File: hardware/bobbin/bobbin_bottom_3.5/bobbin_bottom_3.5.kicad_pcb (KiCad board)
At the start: 2 copper layers, 78.5 x 8.5 mm, 2 parts

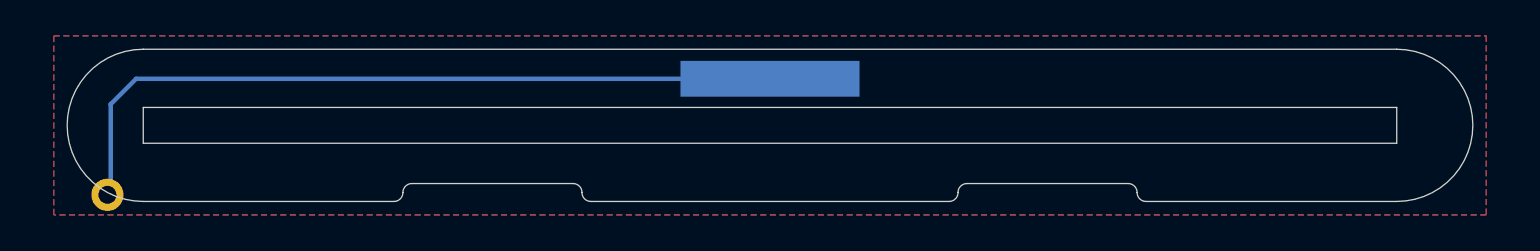
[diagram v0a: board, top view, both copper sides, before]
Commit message: Preamp, Tone Block, Passive, and Bobbin Panel updates
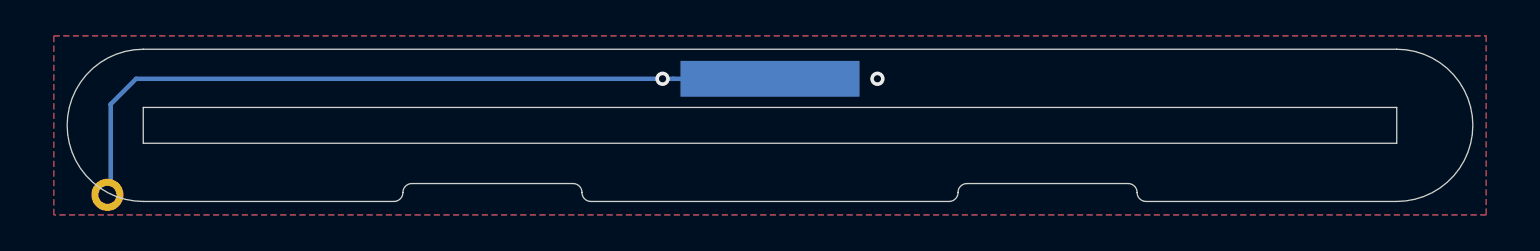
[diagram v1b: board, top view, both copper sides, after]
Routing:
- net GND: vias 0 -> 2
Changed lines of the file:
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@@
     (thickness 1.6)
     (drawings 52)
-    (tracks 6)
+    (tracks 9)
     (zones 0)
     (modules 2)
@@
   (segment (start 93.182276 99.817724) (end 93.182276 104.450033) (width 0.25) (layer B.Cu) (net 1))
   (segment (start 94.6 98.4) (end 93.182276 99.817724) (width 0.25) (layer B.Cu) (net 1))
-  (segment (start 130 98.4) (end 94.6 98.4) (width 0.25) (layer B.Cu) (net 1))
+  (segment (start 130 98.4) (end 124.6 98.4) (width 0.25) (layer B.Cu) (net 1))
+  (segment (start 124.6 98.4) (end 94.6 98.4) (width 0.25) (layer B.Cu) (net 1))
+  (via (at 124 98.4) (size 0.8) (drill 0.4) (layers F.Cu B.Cu) (net 1))
+  (via (at 136 98.4) (size 0.8) (drill 0.4) (layers F.Cu B.Cu) (net 1))
   (zone (net 1) (net_name GND) (layer F.Cu) (hatch edge 0.508)
     (connect_pads yes (clearance 0.25))

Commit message: 3.5 and 4.0 bottom bobbin updates
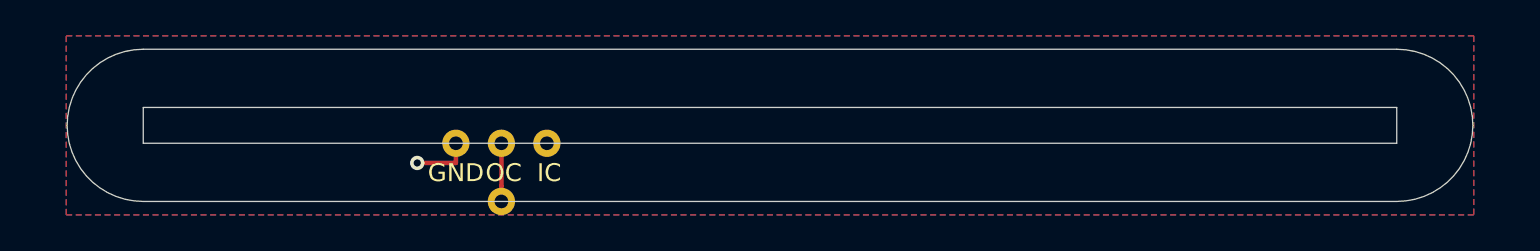
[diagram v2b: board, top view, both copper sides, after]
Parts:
- removed H3: single_pad_smd, cycfi_library:round-single-pad-1.8mm-th
- removed H4: Core GND, cycfi_library:single-pad-10x2
- added J1: Conn_01x01, cycfi_library:xr2-oc-coil-connector, F.Cu at (115.0, 105.2)
- added J2: Conn_01x03, cycfi_library:xr2-coil-connector, F.Cu at (115.0, 102.0)
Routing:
- net GND: track 42.2 -> 2.91 mm, vias 2 -> 1
- net /OC: track 0.00 -> 2.55 mm
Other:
- outline, holes or cut-outs redrawn
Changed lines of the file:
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@@
   (general
     (thickness 1.6)
-    (drawings 52)
-    (tracks 9)
+    (drawings 16)
+    (tracks 5)
     (zones 0)
     (modules 2)
-    (nets 2)
+    (nets 4)
   )
   (page A4)
@@
     (44 Edge.Cuts user)
     (45 Margin user)
-    (46 B.CrtYd user hide)
-    (47 F.CrtYd user hide)
-    (48 B.Fab user hide)
-    (49 F.Fab user hide)
+    (46 B.CrtYd user)
+    (47 F.CrtYd user)
+    (48 B.Fab user)
+    (49 F.Fab user)
   )
   (setup
@@
   (net 0 "")
   (net 1 GND)
+  (net 2 /OC)
+  (net 3 /IC)
   (net_class Default "This is the default net class."
     (clearance 0.2)
@@
     (uvia_dia 0.3)
     (uvia_drill 0.1)
+    (add_net /IC)
+    (add_net /OC)
     (add_net GND)
   )
-  (module cycfi_library:round-single-pad-1.8mm-th (layer F.Cu)
-    (at 93 104.88)
-    (fp_text reference H3 (at 2.73 -0.88) (layer F.SilkS) hide
+  (module cycfi_library:xr2-oc-coil-connector (layer F.Cu)
+    (at 115 105.2 180)
+    (fp_text reference J1 (at 0 5.08) (layer F.SilkS) hide
       (effects (font (size 1 1) (thickness 0.15)))
     )
-    (fp_text value single_pad_smd (at 0 -2.54) (layer F.Fab)
+    (fp_text value Conn_01x01 (at 0 -3.81) (layer F.Fab)
       (effects (font (size 1 1) (thickness 0.15)))
     )
-    (pad 1 thru_hole circle (at 0 0) (size 1.8 1.8) (drill 1) (layers *.Cu *.Mask)
-      (net 1 GND))
+    (pad 1 thru_hole circle (at 0 -0.05 180) (size 1.524 1.524) (drill 0.762) (layers *.Cu *.Mask)
+      (net 2 /OC))
   )
-  (module cycfi_library:single-pad-10x2 (layer B.Cu)
-    (at 130 98.4)
-    (fp_text reference H4 (at 3 -0.6) (layer B.SilkS) hide
+  (module cycfi_library:xr2-coil-connector (layer F.Cu)
+    (at 115 102)
+    (fp_text reference J2 (at 0 5.08) (layer F.SilkS) hide
+      (effects (font (size 1 1) (thickness 0.15)))
+    )
+    (fp_text value Conn_01x03 (at 0 -3.81) (layer F.Fab)
+      (effects (font (size 1 1) (thickness 0.15)))
+    )
+    (fp_text user IC (at 2.667 1.651 180) (layer F.SilkS)
+      (effects (font (size 1 1) (thickness 0.15)))
+    )
+    (fp_text user OC (at 0.127 1.651 180) (layer F.SilkS)
+      (effects (font (size 1 1) (thickness 0.15)))
+    )
+    (fp_text user GND (at -2.54 1.651 180) (layer F.SilkS)
+      (effects (font (size 1 1) (thickness 0.15)))
+    )
+    (fp_text user OC (at 0.127 1.651 180) (layer B.SilkS)
       (effects (font (size 1 1) (thickness 0.15)) (justify mirror))
     )
-    (fp_text value "Core GND" (at 0 2.54) (layer B.Fab)
+    (fp_text user GND (at -2.54 1.651 180) (layer B.SilkS)
       (effects (font (size 1 1) (thickness 0.15)) (justify mirror))
     )
-    (pad 1 smd rect (at 0 0) (size 10 2) (layers B.Cu B.Paste B.Mask)
+    (fp_text user IC (at 2.667 1.651 180) (layer B.SilkS)
+      (effects (font (size 1 1) (thickness 0.15)) (justify mirror))
+    )
+    (pad 1 thru_hole circle (at -2.54 0) (size 1.524 1.524) (drill 0.762) (layers *.Cu *.Mask)
       (net 1 GND))
+    (pad 2 thru_hole circle (at 0 0) (size 1.524 1.524) (drill 0.762) (layers *.Cu *.Mask)
+      (net 2 /OC))
+    (pad 3 thru_hole circle (at 2.54 0) (size 1.524 1.524) (drill 0.762) (layers *.Cu *.Mask)
+      (net 3 /IC))
   )
   (gr_line (start 95 102) (end 165 102) (layer Edge.Cuts) (width 0.05))
@@
   (gr_arc (start 95 101) (end 95 96.75) (angle -180) (layer Edge.Cuts) (width 0.05))
   (gr_line (start 165 96.75) (end 95 96.75) (layer Edge.Cuts) (width 0.05))
-  (gr_arc (start 120 104.75) (end 119.5 104.75) (angle -90) (layer Dwgs.User) (width 0.05))
-  (gr_arc (start 119 104.75) (end 119.5 104.75) (angle -90) (layer Dwgs.User) (width 0.05))
   (gr_line (start 165 96.75) (end 95 96.75) (layer Dwgs.User) (width 0.05))
-  (gr_line (start 151 105.25) (end 165 105.25) (layer Dwgs.User) (width 0.05))
-  (gr_line (start 141 104.25) (end 150 104.25) (layer Dwgs.User) (width 0.05))
-  (gr_line (start 120 105.25) (end 140 105.25) (layer Dwgs.User) (width 0.05))
-  (gr_line (start 135 99.399078) (end 135 97.399078) (layer Dwgs.User) (width 0.05))
+  (gr_line (start 95 105.25) (end 165 105.25) (layer Dwgs.User) (width 0.05))
   (gr_line (start 95 100) (end 165 100) (layer Dwgs.User) (width 0.05))
   (gr_line (start 165 100) (end 165 102) (layer Dwgs.User) (width 0.05))
   (gr_line (start 95 102) (end 165 102) (layer Dwgs.User) (width 0.05))
   (gr_line (start 95 100) (end 95 102) (layer Dwgs.User) (width 0.05))
-  (gr_line (start 125 99.399078) (end 125 97.399078) (layer Dwgs.User) (width 0.05))
-  (gr_line (start 125 97.399078) (end 135 97.399078) (layer Dwgs.User) (width 0.05))
-  (gr_line (start 110 104.25) (end 119 104.25) (layer Dwgs.User) (width 0.05))
-  (gr_line (start 94.999999 105.25) (end 109 105.25) (layer Dwgs.User) (width 0.05))
-  (gr_arc (start 151 104.75) (end 150.5 104.75) (angle -90) (layer Dwgs.User) (width 0.05))
-  (gr_line (start 125 99.399078) (end 135 99.399078) (layer Dwgs.User) (width 0.05))
-  (gr_line (start 125 97.399078) (end 135 99.399078) (layer Dwgs.User) (width 0.05))
-  (gr_line (start 125 99.399078) (end 135 97.399078) (layer Dwgs.User) (width 0.05))
-  (gr_line (start 135 99.399078) (end 135 97.399078) (layer Dwgs.User) (width 0.05))
-  (gr_arc (start 140 104.75) (end 140 105.25) (angle -90) (layer Dwgs.User) (width 0.05))
-  (gr_arc (start 109 104.75) (end 109 105.25) (angle -90) (layer Dwgs.User) (width 0.05))
-  (gr_arc (start 150 104.75) (end 150.5 104.75) (angle -90) (layer Dwgs.User) (width 0.05))
-  (gr_arc (start 141 104.75) (end 141 104.25) (angle -90) (layer Dwgs.User) (width 0.05))
-  (gr_line (start 125 97.399078) (end 135 97.399078) (layer Dwgs.User) (width 0.05))
-  (gr_line (start 125 99.399078) (end 125 97.399078) (layer Dwgs.User) (width 0.05))
-  (gr_line (start 125 99.399078) (end 135 99.399078) (layer Dwgs.User) (width 0.05))
-  (gr_arc (start 95 101) (end 93.739043 105.058631) (angle -17.25924264) (layer Dwgs.User) (width 0.05))
-  (gr_arc (start 93.269552 104.88665) (end 93.739043 105.058631) (angle -172.2370133) (layer Dwgs.User) (width 0.05))
   (gr_arc (start 165 101) (end 165 105.25) (angle -180) (layer Dwgs.User) (width 0.05))
-  (gr_arc (start 95 101) (end 95 96.75) (angle -149.2592426) (layer Dwgs.User) (width 0.05))
-  (gr_arc (start 110 104.75) (end 110 104.25) (angle -90) (layer Dwgs.User) (width 0.05))
+  (gr_arc (start 95 101) (end 95 96.75) (angle -180) (layer Dwgs.User) (width 0.05))
   (gr_line (start 165 100) (end 165 102) (layer Edge.Cuts) (width 0.05))
-  (gr_line (start 110 104.25) (end 119 104.25) (layer Edge.Cuts) (width 0.05))
-  (gr_line (start 95 105.25) (end 109 105.25) (layer Edge.Cuts) (width 0.05))
-  (gr_line (start 151 105.25) (end 165 105.25) (layer Edge.Cuts) (width 0.05))
-  (gr_line (start 141 104.25) (end 150 104.25) (layer Edge.Cuts) (width 0.05))
-  (gr_line (start 120 105.25) (end 140 105.25) (layer Edge.Cuts) (width 0.05))
-  (gr_arc (start 120 104.75) (end 119.5 104.75) (angle -90) (layer Edge.Cuts) (width 0.05))
-  (gr_arc (start 119 104.75) (end 119.5 104.75) (angle -90) (layer Edge.Cuts) (width 0.05))
-  (gr_arc (start 110 104.75) (end 110 104.25) (angle -90) (layer Edge.Cuts) (width 0.05))
-  (gr_arc (start 109 104.75) (end 109 105.25) (angle -90) (layer Edge.Cuts) (width 0.05))
+  (gr_line (start 95 105.25) (end 165 105.25) (layer Edge.Cuts) (width 0.05))
   (gr_arc (start 165 101) (end 165 105.25) (angle -180) (layer Edge.Cuts) (width 0.05))
-  (gr_arc (start 151 104.75) (end 150.5 104.75) (angle -90) (layer Edge.Cuts) (width 0.05))
-  (gr_arc (start 150 104.75) (end 150.5 104.75) (angle -90) (layer Edge.Cuts) (width 0.05))
-  (gr_arc (start 141 104.75) (end 141 104.25) (angle -90) (layer Edge.Cuts) (width 0.05))
-  (gr_arc (start 140 104.75) (end 140 105.25) (angle -90) (layer Edge.Cuts) (width 0.05))
-  (segment (start 93.347699 104.5323) (end 93.261637 104.491088) (width 0.25) (layer F.Cu) (net 1))
-  (segment (start 93.362733 104.517267) (end 93.347699 104.5323) (width 0.25) (layer F.Cu) (net 1))
-  (segment (start 93.182276 104.450033) (end 93.154961 104.435903) (width 0.25) (layer F.Cu) (net 1))
-  (segment (start 93.182276 99.817724) (end 93.182276 104.450033) (width 0.25) (layer B.Cu) (net 1))
-  (segment (start 94.6 98.4) (end 93.182276 99.817724) (width 0.25) (layer B.Cu) (net 1))
-  (segment (start 130 98.4) (end 124.6 98.4) (width 0.25) (layer B.Cu) (net 1))
-  (segment (start 124.6 98.4) (end 94.6 98.4) (width 0.25) (layer B.Cu) (net 1))
-  (via (at 124 98.4) (size 0.8) (drill 0.4) (layers F.Cu B.Cu) (net 1))
-  (via (at 136 98.4) (size 0.8) (drill 0.4) (layers F.Cu B.Cu) (net 1))
+  (via (at 110.3 103.1) (size 0.8) (drill 0.4) (layers F.Cu B.Cu) (net 1))
+  (segment (start 112.46 103.1) (end 110.3 103.1) (width 0.25) (layer F.Cu) (net 1))
+  (segment (start 112.46 103.1) (end 112.46 102.35001) (width 0.25) (layer F.Cu) (net 1))
+  (segment (start 115 104.4) (end 115 104.89999) (width 0.25) (layer F.Cu) (net 2))
+  (segment (start 115 102.35001) (end 115 104.4) (width 0.25) (layer F.Cu) (net 2))
   (zone (net 1) (net_name GND) (layer F.Cu) (hatch edge 0.508)
-    (connect_pads yes (clearance 0.25))
+    (connect_pads (clearance 0.25))
     (min_thickness 0.254)
     (fill yes (arc_segments 32) (thermal_gap 0.508) (thermal_bridge_width 0.508))
     (polygon
       (pts
-        (xy 170 106) (xy 90 106) (xy 90 96) (xy 170 96)
+        (xy 169.3 106) (xy 90.7 106) (xy 90.7 96) (xy 169.3 96)
       )
     )
   )
   (zone (net 1) (net_name GND) (layer B.Cu) (hatch edge 0.508)
-    (connect_pads yes (clearance 0.25))
+    (connect_pads (clearance 0.25))
     (min_thickness 0.254)
     (fill yes (arc_segments 32) (thermal_gap 0.508) (thermal_bridge_width 0.508))
     (polygon
       (pts
-        (xy 170 106) (xy 90 106) (xy 90 96) (xy 170 96)
+        (xy 169.3 106) (xy 90.7 106) (xy 90.7 96) (xy 169.3 96)
       )
     )

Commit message: Copied 3.3" files over
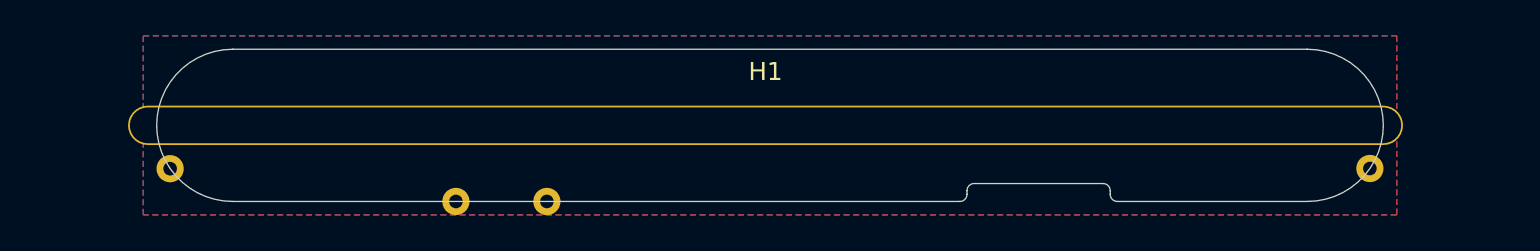
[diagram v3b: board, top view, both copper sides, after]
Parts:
- added H1: single_pad, xr_spectra_library:rail_slot_3.5, F.Cu at (129.8, 101.0)
- added J3: IC, cycfi_library:single-pad-1.52x1.52-th, F.Cu at (96.5, 103.4)
- added J4: IC, cycfi_library:single-pad-1.52x1.52-th, F.Cu at (112.5, 105.2)
- J1: value Conn_01x01 -> OC; footprint cycfi_library:xr2-oc-coil-connector -> cycfi_library:single-pad-1.52x1.52-th
- J2: value Conn_01x03 -> OC; footprint cycfi_library:xr2-coil-connector -> cycfi_library:single-pad-1.52x1.52-th
- moved J2 48.5 mm to (163.5, 103.4), turned to 180 degrees
- moved J1 2.54 mm to (117.5, 105.2)
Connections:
- J2 pad 1: GND -> /OC
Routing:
- net GND: track 2.91 -> 0.00 mm, vias 1 -> 0
- net /OC: track 2.55 -> 0.00 mm
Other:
- board size 78.5 x 8.5 mm -> 68.5 x 8.5 mm
- net class Default removed
